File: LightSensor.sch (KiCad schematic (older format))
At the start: 5 parts, among them U3 VEML6035

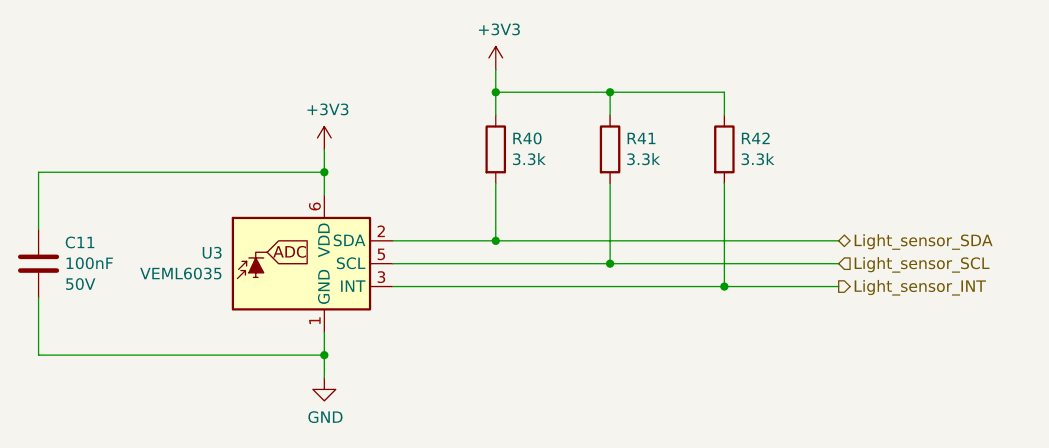
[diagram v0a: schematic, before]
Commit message: Add support components for the FPGA
- Configuration EEPROM
- 20 MHz oscillator
- JTAG debug port connector
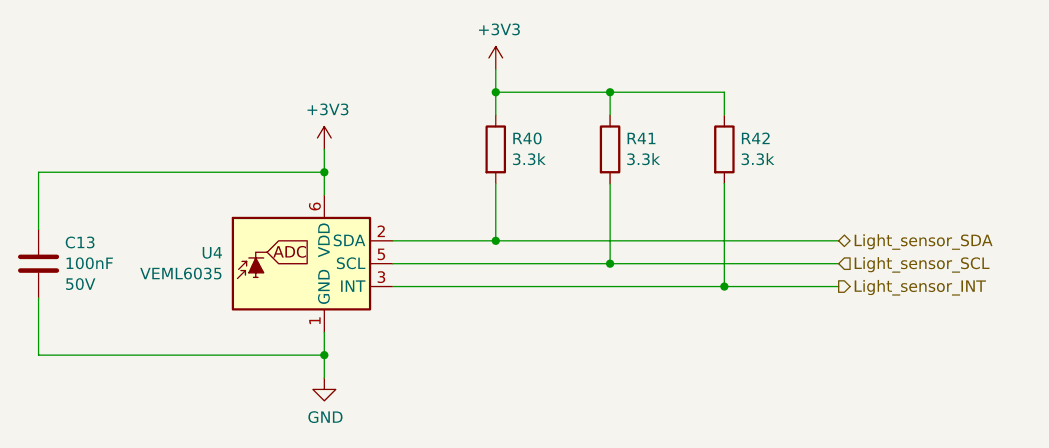
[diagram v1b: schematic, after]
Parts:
- renumbered C11 to C13, U3 to U4
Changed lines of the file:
@@
 $EndDescr
 $Comp
-L LitterRobot:VEML6035 U3
+L LitterRobot:VEML6035 U4
 U 1 1 6062B3AA
 P 5150 3750
-F 0 "U3" H 4806 3796 50  0000 R CNN
+F 0 "U4" H 4806 3796 50  0000 R CNN
 F 1 "VEML6035" H 4806 3705 50  0000 R CNN
 F 2 "LitterRobot:Vishay_VEML6035" H 5150 3250 50  0001 C CNN
@@
 P 5250 4250
 AR Path="/6062F82F" Ref="#PWR?"  Part="1"
-AR Path="/60624089/6062F82F" Ref="#PWR068"  Part="1"
-F 0 "#PWR068" H 5250 4000 50  0001 C CNN
+AR Path="/60624089/6062F82F" Ref="#PWR075"  Part="1"
+F 0 "#PWR075" H 5250 4000 50  0001 C CNN
 F 1 "GND" H 5255 4077 50  0000 C CNN
 F 2 "" H 5250 4250 50  0001 C CNN
@@
 P 5250 3250
 AR Path="/6062F849" Ref="#PWR?"  Part="1"
-AR Path="/60624089/6062F849" Ref="#PWR067"  Part="1"
-F 0 "#PWR067" H 5250 3100 50  0001 C CNN
+AR Path="/60624089/6062F849" Ref="#PWR074"  Part="1"
+F 0 "#PWR074" H 5250 3100 50  0001 C CNN
 F 1 "+3V3" H 5265 3423 50  0000 C CNN
 F 2 "" H 5250 3250 50  0001 C CNN
@@
 P 6000 2900
 AR Path="/60633A13" Ref="#PWR?"  Part="1"
-AR Path="/60624089/60633A13" Ref="#PWR069"  Part="1"
-F 0 "#PWR069" H 6000 2750 50  0001 C CNN
+AR Path="/60624089/60633A13" Ref="#PWR076"  Part="1"
+F 0 "#PWR076" H 6000 2750 50  0001 C CNN
 F 1 "+3V3" H 6015 3073 50  0000 C CNN
 F 2 "" H 6000 2900 50  0001 C CNN
@@
 P 4000 3750
 AR Path="/603F20AB/606362ED" Ref="C?"  Part="1"
-AR Path="/60624089/606362ED" Ref="C11"  Part="1"
-F 0 "C11" H 4115 3841 50  0000 L CNN
+AR Path="/60624089/606362ED" Ref="C13"  Part="1"
+F 0 "C13" H 4115 3841 50  0000 L CNN
 F 1 "100nF" H 4115 3750 50  0000 L CNN
 F 2 "Capacitor_SMD:C_0603_1608Metric" H 4038 3600 50  0001 C CNN
